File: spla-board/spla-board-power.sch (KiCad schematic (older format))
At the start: 53 parts, among them J12 J_POWER, J4 J_POWER2, J7 Barrel_Jack, U14 TLV73311PDBV, U7 ST1S10PHR, U8 ST1S10PHR, U9 TLV73325PDBV

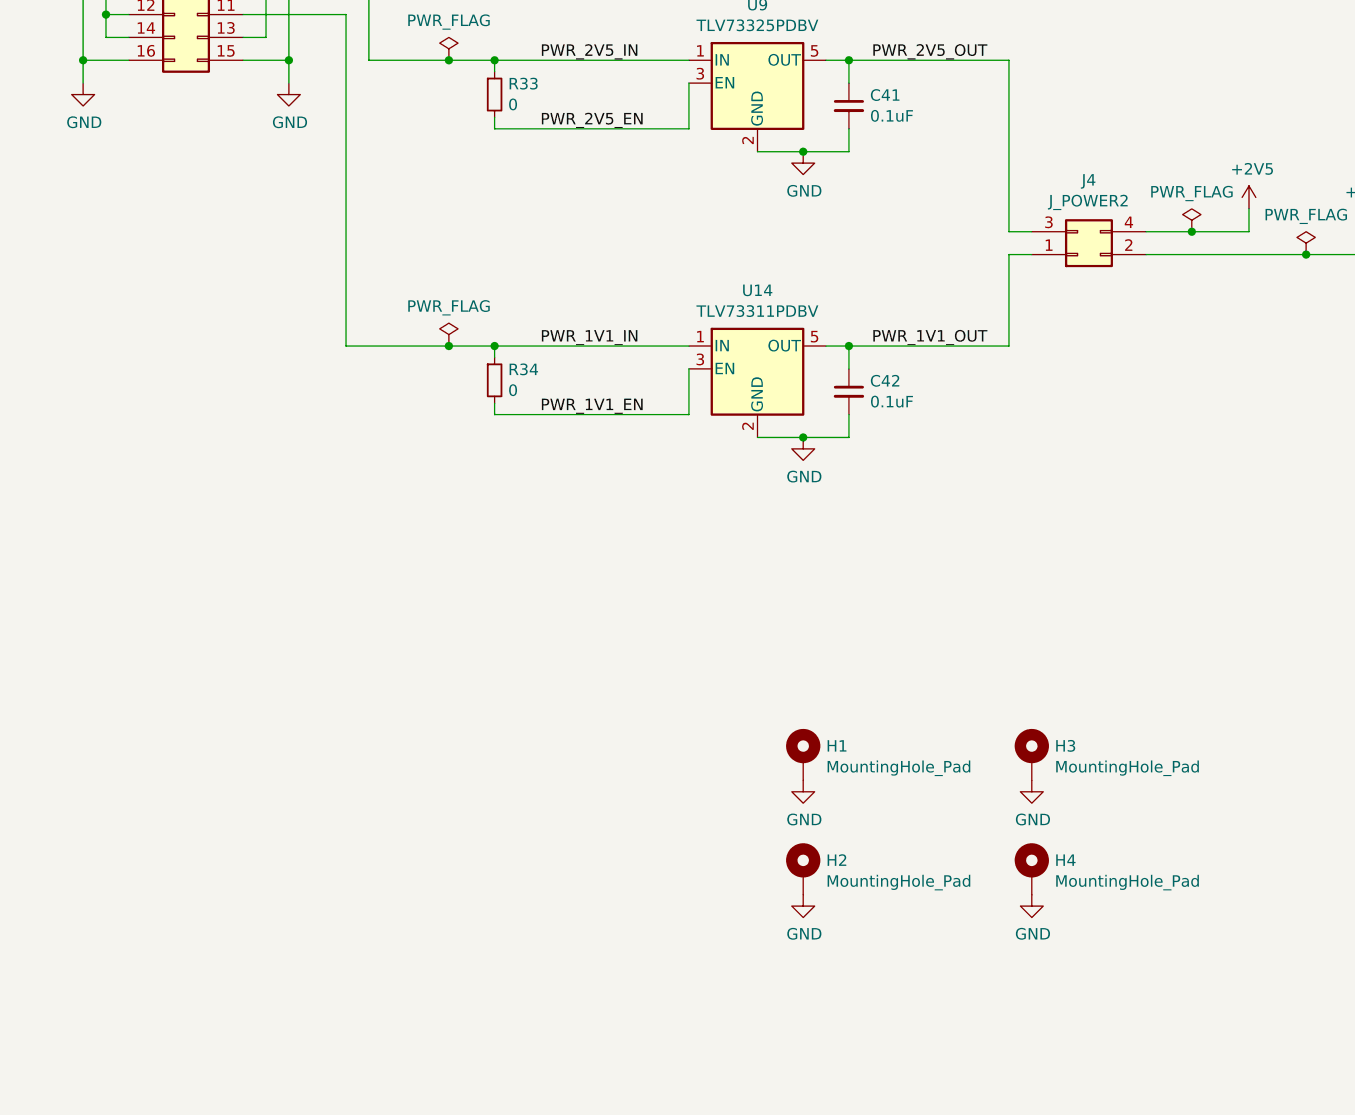
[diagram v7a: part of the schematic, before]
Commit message: schematic/pcb: Add BoM-only symbols.
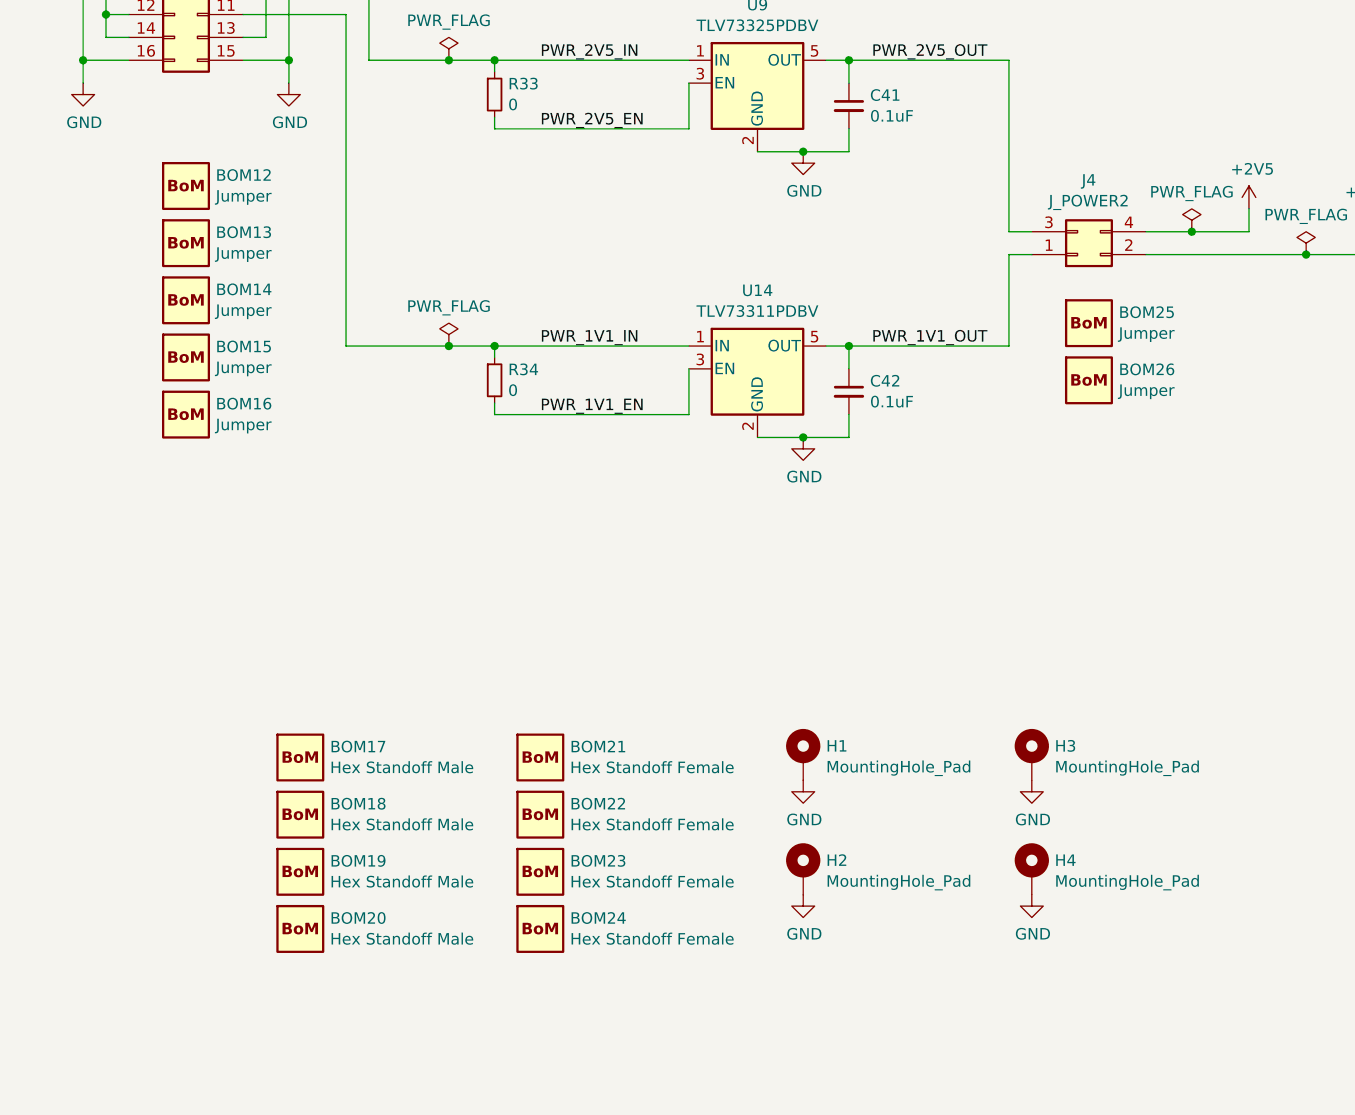
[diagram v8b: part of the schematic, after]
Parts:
- added BOM12, BOM13, BOM14, BOM15, BOM16, BOM25, BOM26: Jumper, SPLA:BoM, symbol SPLA:BomExtra
- added BOM17, BOM18, BOM19, BOM20: Hex Standoff Male, SPLA:BoM, symbol SPLA:BomExtra
- added BOM21, BOM22, BOM23, BOM24: Hex Standoff Female, SPLA:BoM, symbol SPLA:BomExtra
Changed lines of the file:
@@
 Wire Wire Line
 	1450 3550 1450 3650
+$Comp
+L SPLA:BomExtra BOM?
+U 1 1 5EC0FA41
+P 10700 5650
+AR Path="/5E50E589/5EC0FA41" Ref="BOM?"  Part="1"
+AR Path="/5E50D39B/5EC0FA41" Ref="BOM12"  Part="1"
+F 0 "BOM12" H 10830 5696 50  0000 L CNN
+F 1 "Jumper" H 10830 5605 50  0000 L CNN
+F 2 "SPLA:BoM" H 10700 5650 50  0001 C CNN
+F 3 "" H 10700 5650 50  0001 C CNN
+F 4 "S9337-ND" H 10700 5650 50  0001 C CNN "Digikey"
+F 5 "QPC02SXGN-RC" H 10700 5650 50  0001 C CNN "Manufacturer Id"
+	1    10700 5650
+	1    0    0    -1
+$EndComp
+$Comp
+L SPLA:BomExtra BOM?
+U 1 1 5EC1E4A3
+P 14650 6250
+AR Path="/5E50E589/5EC1E4A3" Ref="BOM?"  Part="1"
+AR Path="/5E50D39B/5EC1E4A3" Ref="BOM25"  Part="1"
+F 0 "BOM25" H 14780 6296 50  0000 L CNN
+F 1 "Jumper" H 14780 6205 50  0000 L CNN
+F 2 "SPLA:BoM" H 14650 6250 50  0001 C CNN
+F 3 "" H 14650 6250 50  0001 C CNN
+F 4 "S9337-ND" H 14650 6250 50  0001 C CNN "Digikey"
+F 5 "QPC02SXGN-RC" H 14650 6250 50  0001 C CNN "Manufacturer Id"
+	1    14650 6250
+	1    0    0    -1
+$EndComp
+$Comp
+L SPLA:BomExtra BOM?
+U 1 1 5EC2D1EF
+P 14650 6500
+AR Path="/5E50E589/5EC2D1EF" Ref="BOM?"  Part="1"
+AR Path="/5E50D39B/5EC2D1EF" Ref="BOM26"  Part="1"
+F 0 "BOM26" H 14780 6546 50  0000 L CNN
+F 1 "Jumper" H 14780 6455 50  0000 L CNN
+F 2 "SPLA:BoM" H 14650 6500 50  0001 C CNN
+F 3 "" H 14650 6500 50  0001 C CNN
+F 4 "S9337-ND" H 14650 6500 50  0001 C CNN "Digikey"
+F 5 "QPC02SXGN-RC" H 14650 6500 50  0001 C CNN "Manufacturer Id"
+	1    14650 6500
+	1    0    0    -1
+$EndComp
+$Comp
+L SPLA:BomExtra BOM?
+U 1 1 5EC3BD64
+P 10700 5900
+AR Path="/5E50E589/5EC3BD64" Ref="BOM?"  Part="1"
+AR Path="/5E50D39B/5EC3BD64" Ref="BOM13"  Part="1"
+F 0 "BOM13" H 10830 5946 50  0000 L CNN
+F 1 "Jumper" H 10830 5855 50  0000 L CNN
+F 2 "SPLA:BoM" H 10700 5900 50  0001 C CNN
+F 3 "" H 10700 5900 50  0001 C CNN
+F 4 "S9337-ND" H 10700 5900 50  0001 C CNN "Digikey"
+F 5 "QPC02SXGN-RC" H 10700 5900 50  0001 C CNN "Manufacturer Id"
+	1    10700 5900
+	1    0    0    -1
+$EndComp
+$Comp
+L SPLA:BomExtra BOM?
+U 1 1 5EC59424
+P 10700 6150
+AR Path="/5E50E589/5EC59424" Ref="BOM?"  Part="1"
+AR Path="/5E50D39B/5EC59424" Ref="BOM14"  Part="1"
+F 0 "BOM14" H 10830 6196 50  0000 L CNN
+F 1 "Jumper" H 10830 6105 50  0000 L CNN
+F 2 "SPLA:BoM" H 10700 6150 50  0001 C CNN
+F 3 "" H 10700 6150 50  0001 C CNN
+F 4 "S9337-ND" H 10700 6150 50  0001 C CNN "Digikey"
+F 5 "QPC02SXGN-RC" H 10700 6150 50  0001 C CNN "Manufacturer Id"
+	1    10700 6150
+	1    0    0    -1
+$EndComp
+$Comp
+L SPLA:BomExtra BOM?
+U 1 1 5EC59430
+P 10700 6400
+AR Path="/5E50E589/5EC59430" Ref="BOM?"  Part="1"
+AR Path="/5E50D39B/5EC59430" Ref="BOM15"  Part="1"
+F 0 "BOM15" H 10830 6446 50  0000 L CNN
+F 1 "Jumper" H 10830 6355 50  0000 L CNN
+F 2 "SPLA:BoM" H 10700 6400 50  0001 C CNN
+F 3 "" H 10700 6400 50  0001 C CNN
+F 4 "S9337-ND" H 10700 6400 50  0001 C CNN "Digikey"
+F 5 "QPC02SXGN-RC" H 10700 6400 50  0001 C CNN "Manufacturer Id"
+	1    10700 6400
+	1    0    0    -1
+$EndComp
+$Comp
+L SPLA:BomExtra BOM?
+U 1 1 5EC6835C
+P 10700 6650
+AR Path="/5E50E589/5EC6835C" Ref="BOM?"  Part="1"
+AR Path="/5E50D39B/5EC6835C" Ref="BOM16"  Part="1"
+F 0 "BOM16" H 10830 6696 50  0000 L CNN
+F 1 "Jumper" H 10830 6605 50  0000 L CNN
+F 2 "SPLA:BoM" H 10700 6650 50  0001 C CNN
+F 3 "" H 10700 6650 50  0001 C CNN
+F 4 "S9337-ND" H 10700 6650 50  0001 C CNN "Digikey"
+F 5 "QPC02SXGN-RC" H 10700 6650 50  0001 C CNN "Manufacturer Id"
+	1    10700 6650
+	1    0    0    -1
+$EndComp
+$Comp
+L SPLA:BomExtra BOM?
+U 1 1 5EC85D97
+P 11200 8150
+AR Path="/5E50E589/5EC85D97" Ref="BOM?"  Part="1"
+AR Path="/5E50D39B/5EC85D97" Ref="BOM17"  Part="1"
+F 0 "BOM17" H 11330 8196 50  0000 L CNN
+F 1 "Hex Standoff Male" H 11330 8105 50  0000 L CNN
+F 2 "SPLA:BoM" H 11200 8150 50  0001 C CNN
+F 3 "" H 11200 8150 50  0001 C CNN
+F 4 "732-12823-ND" H 11200 8150 50  0001 C CNN "Digikey"
+F 5 "971350366" H 11200 8150 50  0001 C CNN "Manufacturer Id"
+	1    11200 8150
+	1    0    0    -1
+$EndComp
+$Comp
+L SPLA:BomExtra BOM?
+U 1 1 5ECA37F7
+P 11200 8400
+AR Path="/5E50E589/5ECA37F7" Ref="BOM?"  Part="1"
+AR Path="/5E50D39B/5ECA37F7" Ref="BOM18"  Part="1"
+F 0 "BOM18" H 11330 8446 50  0000 L CNN
+F 1 "Hex Standoff Male" H 11330 8355 50  0000 L CNN
+F 2 "SPLA:BoM" H 11200 8400 50  0001 C CNN
+F 3 "" H 11200 8400 50  0001 C CNN
+F 4 "732-12823-ND" H 11200 8400 50  0001 C CNN "Digikey"
+F 5 "971350366" H 11200 8400 50  0001 C CNN "Manufacturer Id"
+	1    11200 8400
+	1    0    0    -1
+$EndComp
+$Comp
+L SPLA:BomExtra BOM?
+U 1 1 5ECB250A
+P 11200 8650
+AR Path="/5E50E589/5ECB250A" Ref="BOM?"  Part="1"
+AR Path="/5E50D39B/5ECB250A" Ref="BOM19"  Part="1"
+F 0 "BOM19" H 11330 8696 50  0000 L CNN
+F 1 "Hex Standoff Male" H 11330 8605 50  0000 L CNN
+F 2 "SPLA:BoM" H 11200 8650 50  0001 C CNN
+F 3 "" H 11200 8650 50  0001 C CNN
+F 4 "732-12823-ND" H 11200 8650 50  0001 C CNN "Digikey"
+F 5 "971350366" H 11200 8650 50  0001 C CNN "Manufacturer Id"
+	1    11200 8650
+	1    0    0    -1
+$EndComp
+$Comp
+L SPLA:BomExtra BOM?
+U 1 1 5ECB2516
+P 11200 8900
+AR Path="/5E50E589/5ECB2516" Ref="BOM?"  Part="1"
+AR Path="/5E50D39B/5ECB2516" Ref="BOM20"  Part="1"
+F 0 "BOM20" H 11330 8946 50  0000 L CNN
+F 1 "Hex Standoff Male" H 11330 8855 50  0000 L CNN
+F 2 "SPLA:BoM" H 11200 8900 50  0001 C CNN
+F 3 "" H 11200 8900 50  0001 C CNN
+F 4 "732-12823-ND" H 11200 8900 50  0001 C CNN "Digikey"
+F 5 "971350366" H 11200 8900 50  0001 C CNN "Manufacturer Id"
+	1    11200 8900
+	1    0    0    -1
+$EndComp
+$Comp
+L SPLA:BomExtra BOM?
+U 1 1 5ECC13CC
+P 12250 8150
+AR Path="/5E50E589/5ECC13CC" Ref="BOM?"  Part="1"
+AR Path="/5E50D39B/5ECC13CC" Ref="BOM21"  Part="1"
+F 0 "BOM21" H 12380 8196 50  0000 L CNN
+F 1 "Hex Standoff Female" H 12380 8105 50  0000 L CNN
+F 2 "SPLA:BoM" H 12250 8150 50  0001 C CNN
+F 3 "" H 12250 8150 50  0001 C CNN
+F 4 "732-12808-ND" H 12250 8150 50  0001 C CNN "Digikey"
+F 5 "970350366" H 12250 8150 50  0001 C CNN "Manufacturer Id"
+	1    12250 8150
+	1    0    0    -1
+$EndComp
+$Comp
+L SPLA:BomExtra BOM?
+U 1 1 5ECD0146
+P 12250 8400
+AR Path="/5E50E589/5ECD0146" Ref="BOM?"  Part="1"
+AR Path="/5E50D39B/5ECD0146" Ref="BOM22"  Part="1"
+F 0 "BOM22" H 12380 8446 50  0000 L CNN
+F 1 "Hex Standoff Female" H 12380 8355 50  0000 L CNN
+F 2 "SPLA:BoM" H 12250 8400 50  0001 C CNN
+F 3 "" H 12250 8400 50  0001 C CNN
+F 4 "732-12808-ND" H 12250 8400 50  0001 C CNN "Digikey"
+F 5 "970350366" H 12250 8400 50  0001 C CNN "Manufacturer Id"
+	1    12250 8400
+	1    0    0    -1
+$EndComp
+$Comp
+L SPLA:BomExtra BOM?
+U 1 1 5ECDECF4
+P 12250 8650
+AR Path="/5E50E589/5ECDECF4" Ref="BOM?"  Part="1"
+AR Path="/5E50D39B/5ECDECF4" Ref="BOM23"  Part="1"
+F 0 "BOM23" H 12380 8696 50  0000 L CNN
+F 1 "Hex Standoff Female" H 12380 8605 50  0000 L CNN
+F 2 "SPLA:BoM" H 12250 8650 50  0001 C CNN
+F 3 "" H 12250 8650 50  0001 C CNN
+F 4 "732-12808-ND" H 12250 8650 50  0001 C CNN "Digikey"
+F 5 "970350366" H 12250 8650 50  0001 C CNN "Manufacturer Id"
+	1    12250 8650
+	1    0    0    -1
+$EndComp
+$Comp
+L SPLA:BomExtra BOM?
+U 1 1 5ECDED00
+P 12250 8900
+AR Path="/5E50E589/5ECDED00" Ref="BOM?"  Part="1"
+AR Path="/5E50D39B/5ECDED00" Ref="BOM24"  Part="1"
+F 0 "BOM24" H 12380 8946 50  0000 L CNN
+F 1 "Hex Standoff Female" H 12380 8855 50  0000 L CNN
+F 2 "SPLA:BoM" H 12250 8900 50  0001 C CNN
+F 3 "" H 12250 8900 50  0001 C CNN
+F 4 "732-12808-ND" H 12250 8900 50  0001 C CNN "Digikey"
+F 5 "970350366" H 12250 8900 50  0001 C CNN "Manufacturer Id"
+	1    12250 8900
+	1    0    0    -1
+$EndComp
 $EndSCHEMATC
